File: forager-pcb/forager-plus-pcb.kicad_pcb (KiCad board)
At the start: 2 copper layers, 114.6 x 96.3 mm, 27 parts, among them J2 Conn_01x02_Pin, U1 XIAO nRF52840 Plus

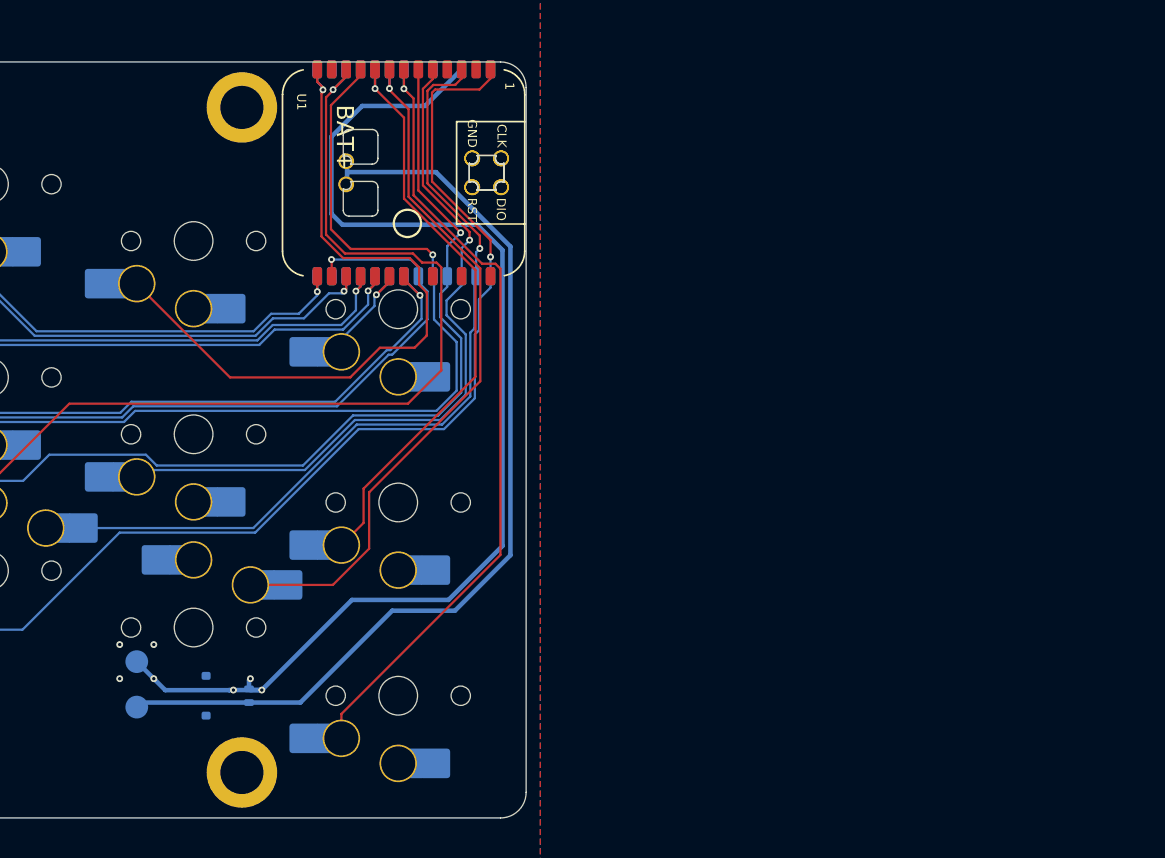
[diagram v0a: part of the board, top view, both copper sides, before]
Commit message: Column 4 now with reversible choc v1 switch footprints
Using ceoloide's ergogen-footprints/switch_choc_v1_v2.js
in v1 only mode (not enough space near controller for v2).
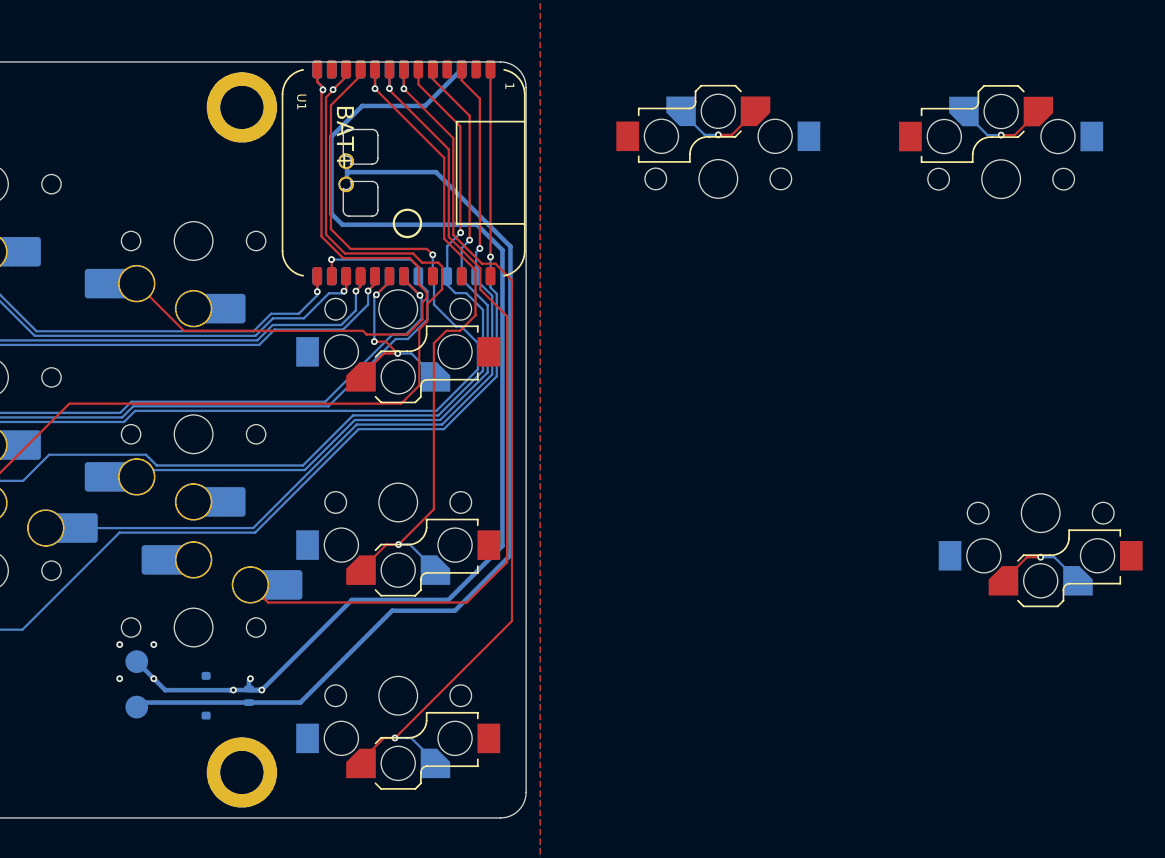
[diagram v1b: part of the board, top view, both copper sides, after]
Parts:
- removed RCH10, RCH15, RCH5: ChocHS, Custom:SW_choc_v1_HS_MBK
- added S3: , ceoloide:switch_choc_v1_v2, B.Cu at (107.0, -11.0)
- added S3: , ceoloide:switch_choc_v1_v2, B.Cu at (160.0, -39.4)
- added S3: , ceoloide:switch_choc_v1_v2, B.Cu at (163.5, -10.1)
- added S3: , ceoloide:switch_choc_v1_v2, B.Cu at (107.0, -28.0)
- added S3: , ceoloide:switch_choc_v1_v2, B.Cu at (107.0, 6.00)
- added S3: , ceoloide:switch_choc_v1_v2, B.Cu at (135.2, -39.5)
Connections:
- U1 pad 9: (no net) -> GND
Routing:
- net (no net): track 0.00 -> 24.8 mm, vias 0 -> 3
- net RB3: track 63.0 -> 72.7 mm
- net RT4: track 9.39 -> 18.2 mm, vias 1 -> 3
- net RB4: track 70.6 -> 77.7 mm, vias 1 -> 2
- net RM4: track 52.1 -> 59.1 mm, vias 1 -> 2
- net RH1: track 126.1 -> 120.0 mm
- net RT3: track 63.4 -> 59.2 mm
- net RB2: track 75.3 -> 73.0 mm
- net RB1: track 93.0 -> 94.6 mm
- net RM0: track 84.9 -> 83.6 mm
- net RB0: track 130.0 -> 131.3 mm
- net RH0: track 152.7 -> 151.7 mm

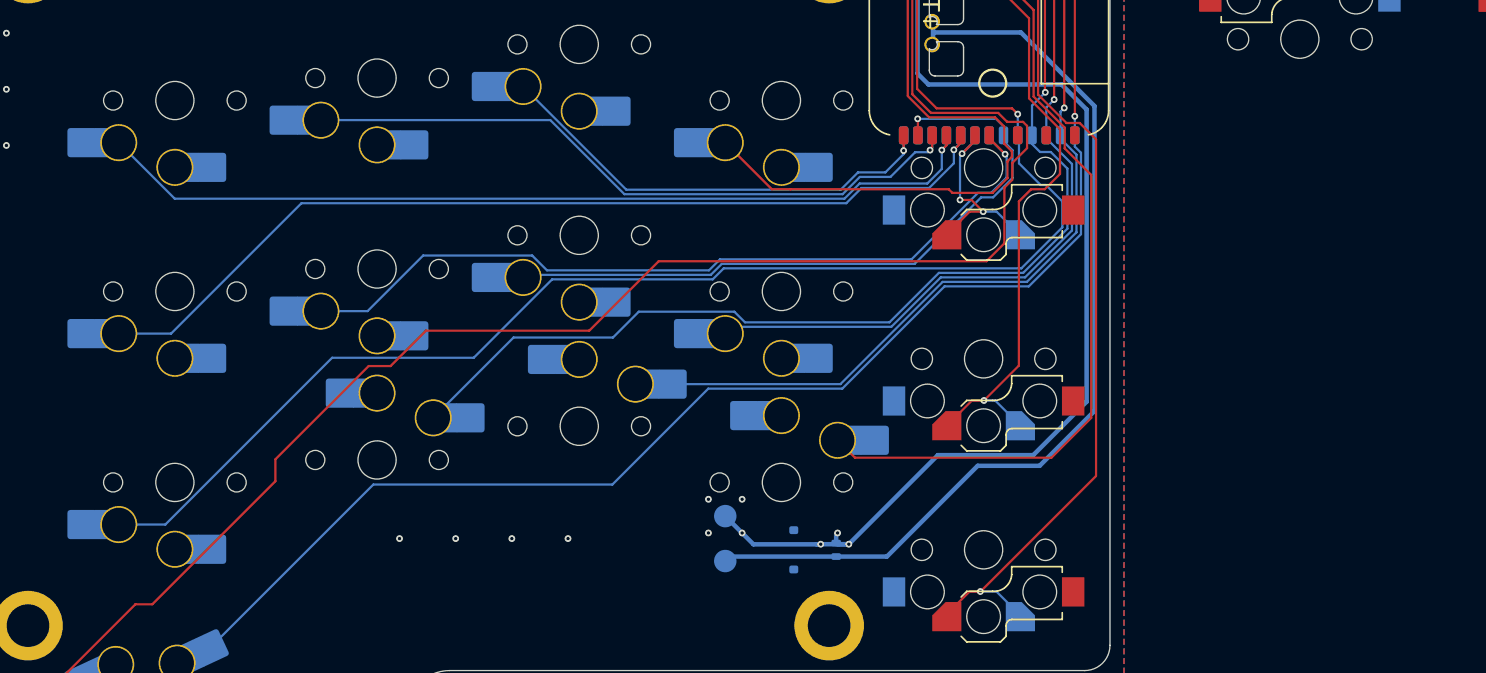
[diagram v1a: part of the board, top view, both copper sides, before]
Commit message: More reversible switches
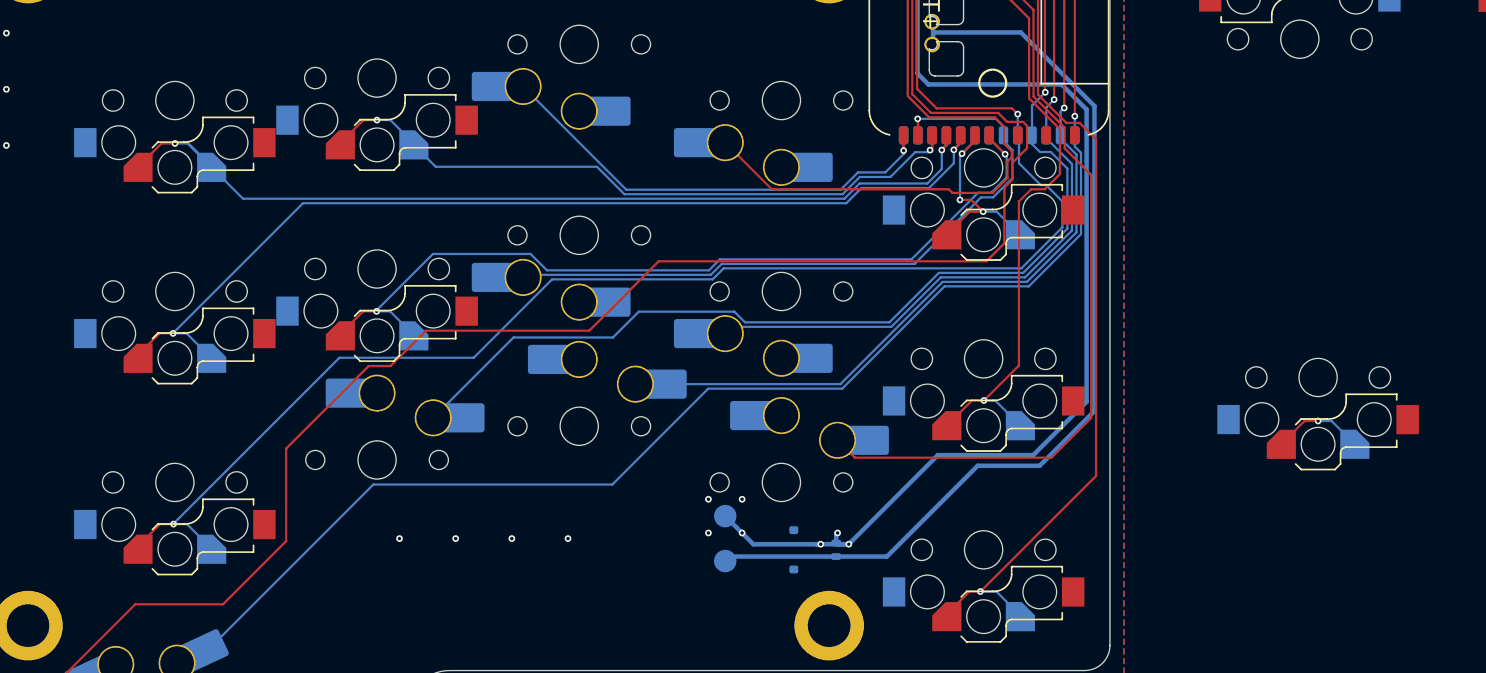
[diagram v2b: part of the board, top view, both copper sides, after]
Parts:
- removed RCH1, RCH11, RCH2, RCH6, RCH7: ChocHS, Custom:SW_choc_v1_HS_MBK
- added S3: , ceoloide:switch_choc_v1_v2, B.Cu at (136.8, -9.35)
- added S3: , ceoloide:switch_choc_v1_v2, B.Cu at (53.0, -36.0)
- added S3: , ceoloide:switch_choc_v1_v2, B.Cu at (53.0, -19.0)
- added S3: , ceoloide:switch_choc_v1_v2, B.Cu at (35.0, -17.0)
- added S3: , ceoloide:switch_choc_v1_v2, B.Cu at (35.0, -34.0)
- added S3: , ceoloide:switch_choc_v1_v2, B.Cu at (35.0, 0.00)
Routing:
- net (no net): track 24.8 -> 33.1 mm, vias 3 -> 4
- net RH0: track 151.7 -> 155.4 mm
- net RM1: track 73.2 -> 76.8 mm, vias 1 -> 2
- net RM0: track 83.6 -> 87.0 mm, vias 1 -> 2
- net RB0: track 131.3 -> 134.8 mm, vias 1 -> 2
- net RT0: track 81.1 -> 83.3 mm, vias 1 -> 2
- net RT1: track 61.4 -> 60.9 mm, vias 1 -> 2

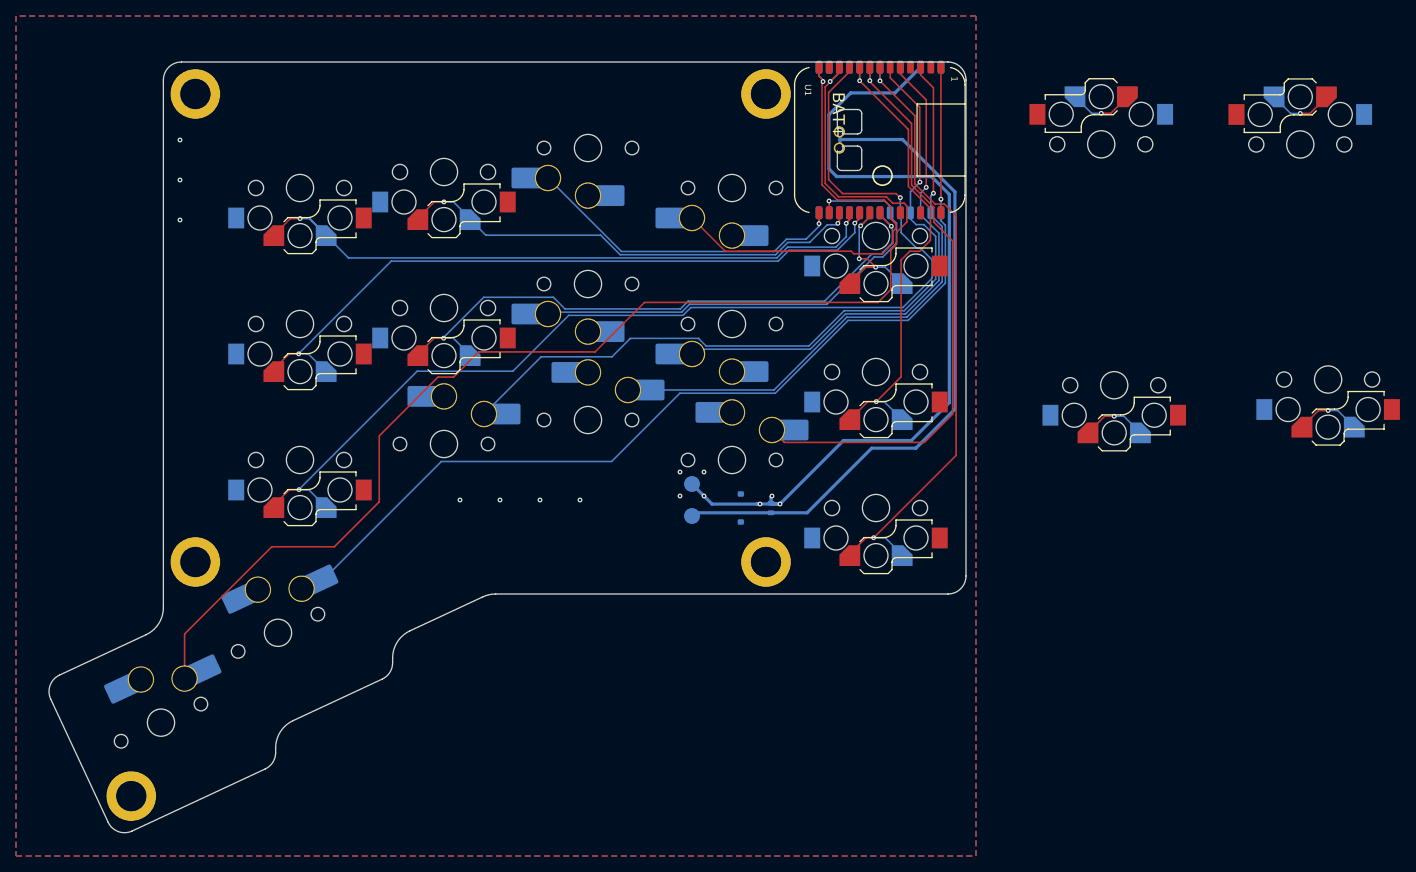
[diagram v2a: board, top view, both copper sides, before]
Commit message: Now all reversible switches - fighting ground plane
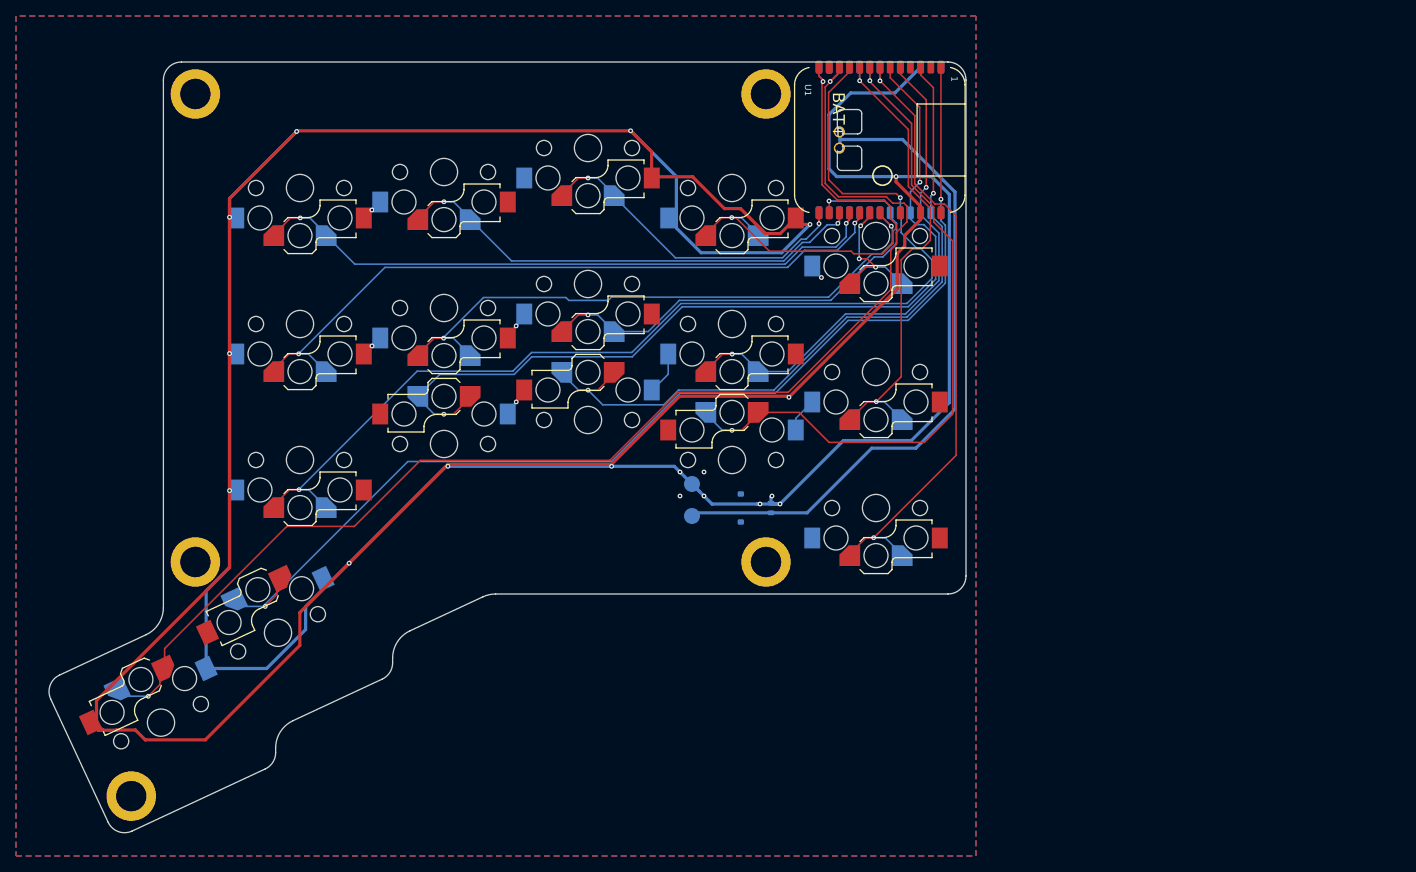
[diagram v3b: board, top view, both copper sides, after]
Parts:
- removed RCH12, RCH13, RCH14, RCH16, RCH17, RCH3, RCH4, RCH8, RCH9: ChocHS, Custom:SW_choc_v1_HS_MBK
- removed the S3 at (136.8, -9.35)
- removed the S3 at (135.2, -39.5)
- removed the S3 at (163.5, -10.1)
- added S3: , ceoloide:switch_choc_v1_v2, B.Cu at (71.0, -39.0)
- added S3: , ceoloide:switch_choc_v1_v2, B.Cu at (89.0, 0.00)
- added S3: , ceoloide:switch_choc_v1_v2, B.Cu at (53.0, -2.00)
- added S3: , ceoloide:switch_choc_v1_v2, B.Cu at (89.0, -34.0)
- added S3: , ceoloide:switch_choc_v1_v2, B.Cu at (17.6, 32.8)
- added S3: , ceoloide:switch_choc_v1_v2, B.Cu at (89.0, -17.0)
- added S3: , ceoloide:switch_choc_v1_v2, B.Cu at (71.0, -5.00)
- added S3: , ceoloide:switch_choc_v1_v2, B.Cu at (71.0, -22.0)
- moved S3 141.6 mm to (32.3, 21.6), turned to 25 degrees
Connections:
- net RBAT renamed BAT
- J2 pad 2: RGND -> GND
- S3 pad 1: (no net) -> RH1
- TP4 pad 1: RGND -> GND
- U1 pad 9: RGND -> GND
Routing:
- net GND: track 0.00 -> 604.9 mm, vias 0 -> 23
- net RGND: track 103.6 -> 0.00 mm, vias 14 -> 0
- net (no net): track 33.1 -> 0.00 mm, vias 4 -> 0
- net RH1: track 120.0 -> 135.8 mm, vias 1 -> 2
- net RB1: track 94.6 -> 109.5 mm, vias 1 -> 2
- net RB2: track 73.0 -> 87.8 mm, vias 1 -> 2
- net RB3: track 72.7 -> 84.9 mm, vias 1 -> 2
- net RT3: track 59.2 -> 62.5 mm, vias 1 -> 2
- net RT0: track 83.3 -> 80.8 mm
- net RH0: track 155.4 -> 157.4 mm, vias 1 -> 2
- net RM3: track 62.8 -> 64.6 mm, vias 1 -> 2
- net RM2: track 60.7 -> 61.9 mm, vias 1 -> 2
- net RM1: track 76.8 -> 75.9 mm
- net RT2: track 42.0 -> 41.7 mm, vias 1 -> 2
- added copper zone on B.Cu, net GND
- added copper zone on F.Cu, net GND
- removed copper zone on B.Cu, net RGND
- removed copper zone on F.Cu, net RGND

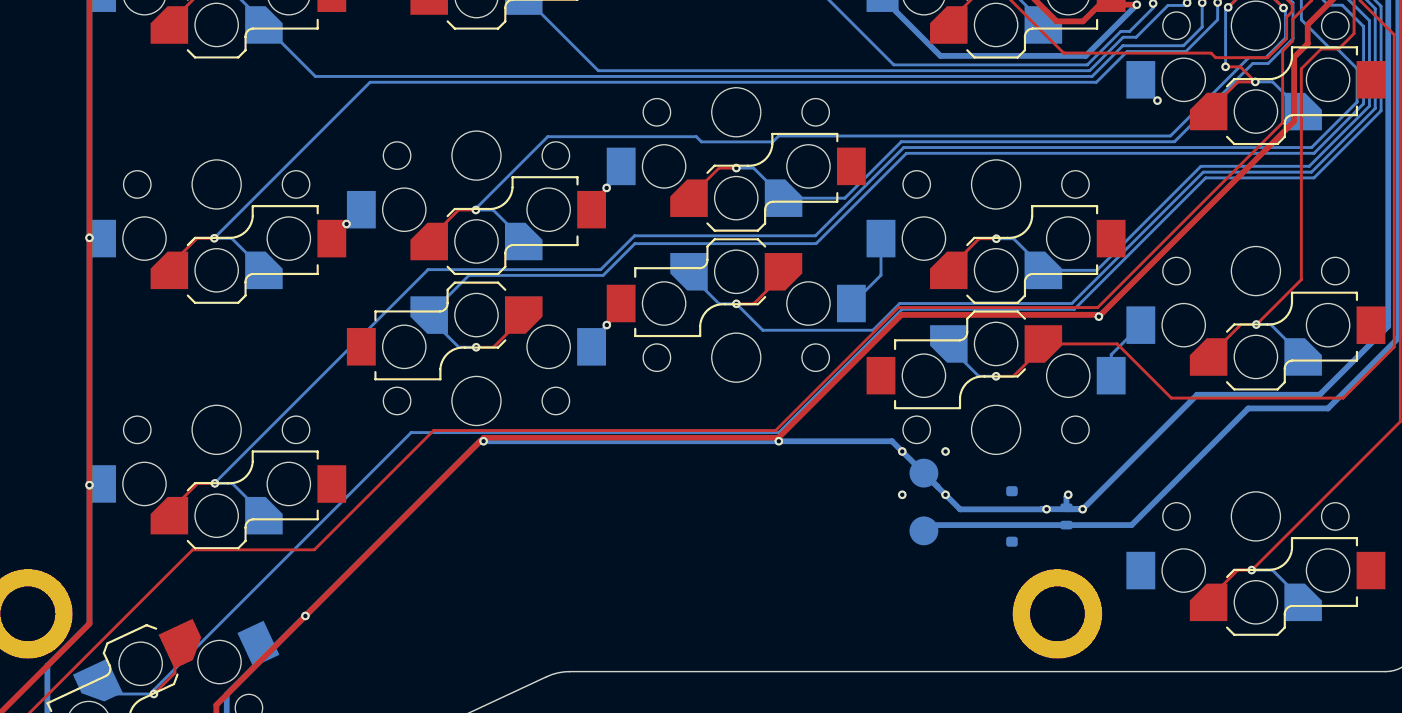
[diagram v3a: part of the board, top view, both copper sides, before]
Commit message: Solved ground plane with explicit tracks
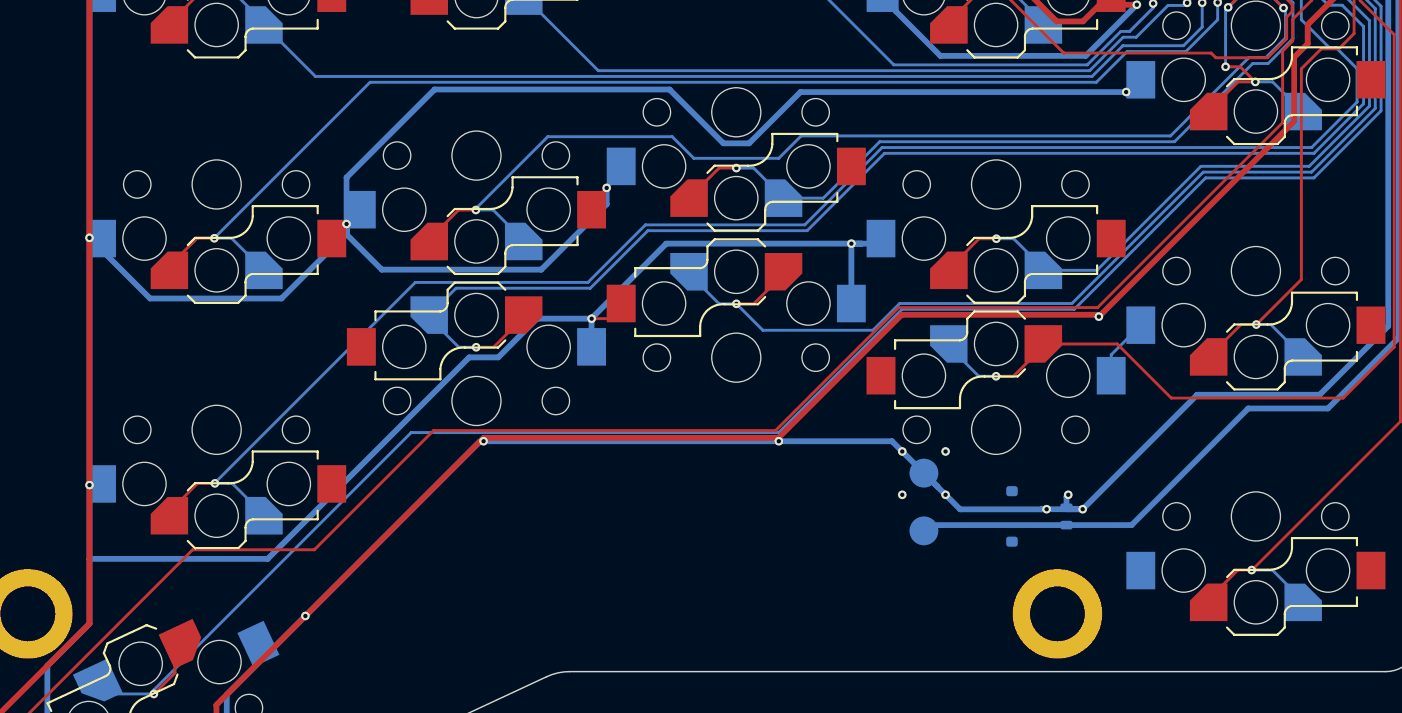
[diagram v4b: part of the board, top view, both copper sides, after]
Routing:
- net GND: track 604.9 -> 777.8 mm, vias 23 -> 24
- net RM1: track 75.9 -> 76.8 mm
